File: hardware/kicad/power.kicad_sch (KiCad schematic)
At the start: 0 parts

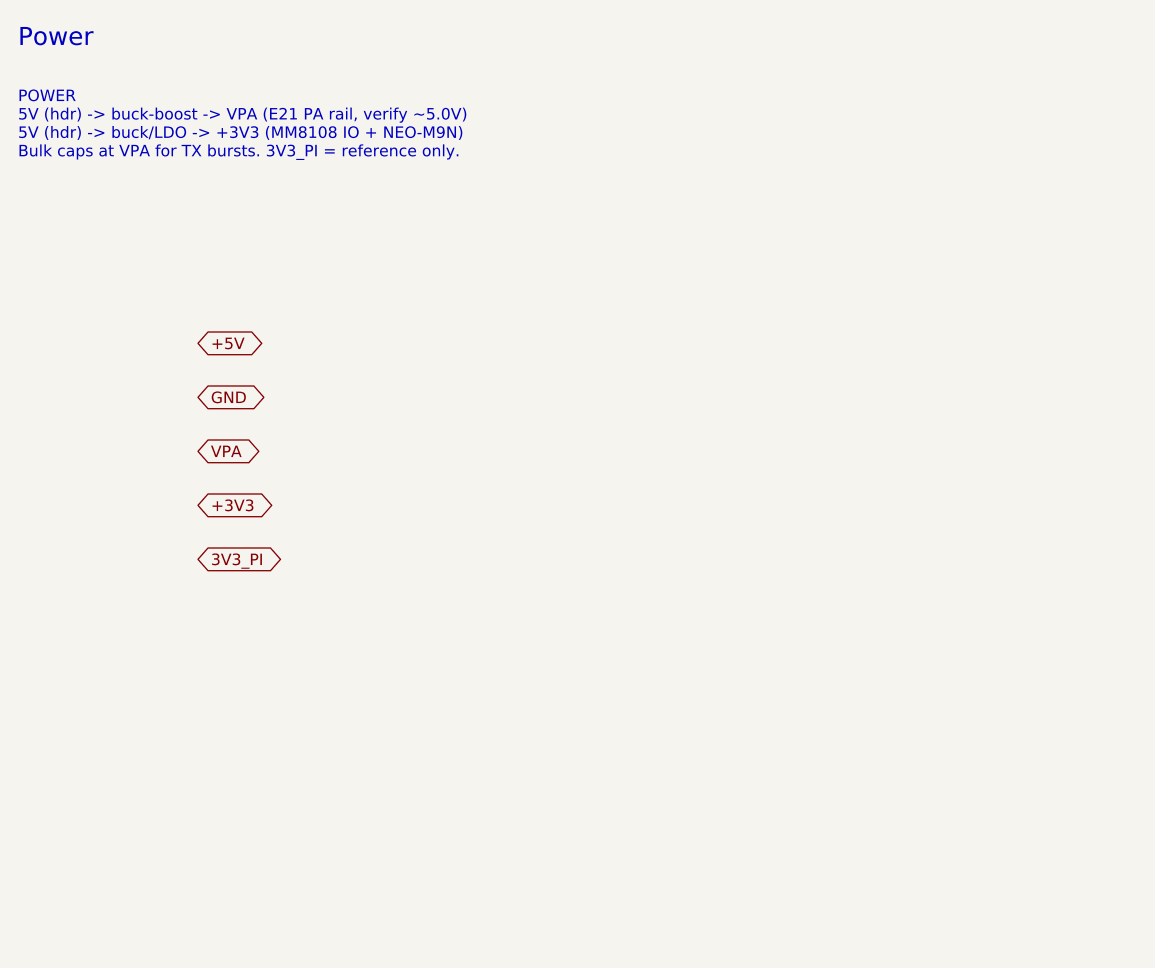
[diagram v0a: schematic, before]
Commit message: Deepen design to component level + fix EEPROM power rail
- Fix: HAT ID EEPROM (U6) now powered from Pi header 3V3 (3V3_PI, pin 1)
  so it is readable at boot before the HAT's own 3V3 comes up (was
  incorrectly on the HAT 3V3 regulator).
- Add docs/SCHEMATIC.md: component-level subcircuits for every block
  (refdes + values + nets) — buck-boost/3V3 FB dividers, MM8108 SPI
  termination/pulls, E21 RF DC-blocks/attenuator pad/T-R pulldowns,
  NEO-M9N active-antenna bias via VCC_RF, ID EEPROM (WP default).
- Add docs/BRINGUP.md: stage-gated power-on + RF test plan (don't key
  the 1W PA until rails/drive-level/FEM-timing verified).
- Add GNSS VCC_RF antenna bias + +3V3_GNSS ferrite to the net list.
- Enrich KiCad sub-sheets with per-block refdes notes and the new nets;
  regenerate scaffold (KiCad 10 format, S-expression balance re-checked).
- BOM: concrete passives (RF DC-blocks, attenuator pad, ferrite, TVS,
  FB dividers, WP jumper).

https://claude.ai/code/session_015nkkW85U3sPf5mcvrsMw7T
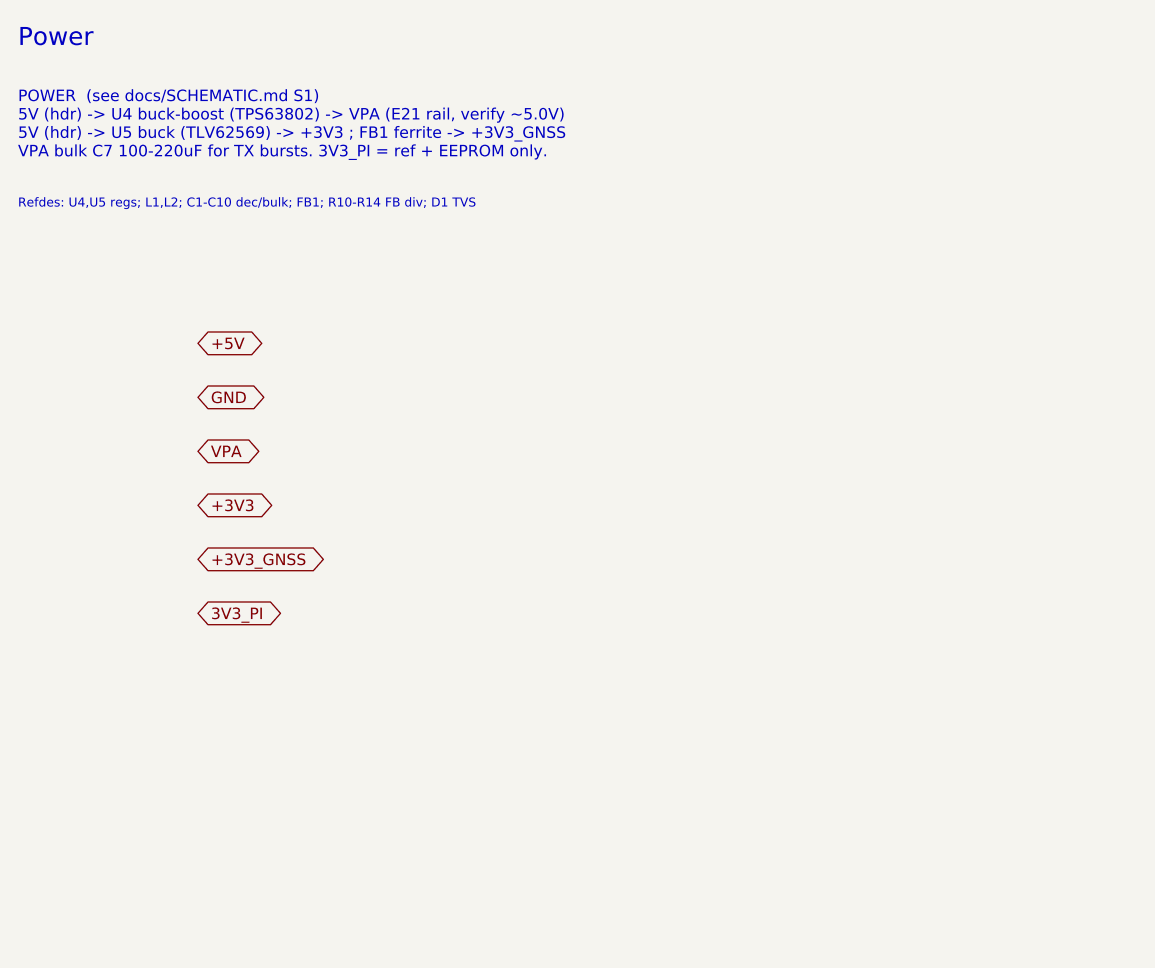
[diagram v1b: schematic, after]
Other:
- note added: "POWER (see docs/SCHEMATIC.md S1) 5V (hdr) -> U4 buck-boost (TPS63802) -> VPA (E21 rail, verify ~5.0V) 5V (hdr) -> U5 buck (TLV62569) -> +3V3 ; FB1 ferrite -> +3V3_GNSS VPA bulk C7 100-220uF for TX bursts. 3V3_PI = ref + EEPROM only."
- note added: "Refdes: U4,U5 regs; L1,L2; C1-C10 dec/bulk; FB1; R10-R14 FB div; D1 TVS"
- note removed: "POWER 5V (hdr) -> buck-boost -> VPA (E21 PA rail, verify ~5.0V) 5V (hdr) -> buck/LDO -> +3V3 (MM8108 IO + NEO-M9N) Bulk caps at VPA for TX bursts. 3V3_PI = reference only."
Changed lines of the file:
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@@
 	(paper "A4")
 	(text "Power" (exclude_from_sim no) (at 20 15 0) (effects (font (size 2 2) (thickness 0.3)) (justify left top)))
-	(text "POWER\n5V (hdr) -> buck-boost -> VPA (E21 PA rail, verify ~5.0V)\n5V (hdr) -> buck/LDO -> +3V3 (MM8108 IO + NEO-M9N)\nBulk caps at VPA for TX bursts. 3V3_PI = reference only." (exclude_from_sim no) (at 20 22 0) (effects (font (size 1.27 1.27)) (justify left top)))
+	(text "POWER  (see docs/SCHEMATIC.md S1)\n5V (hdr) -> U4 buck-boost (TPS63802) -> VPA (E21 rail, verify ~5.0V)\n5V (hdr) -> U5 buck (TLV62569) -> +3V3 ; FB1 ferrite -> +3V3_GNSS\nVPA bulk C7 100-220uF for TX bursts. 3V3_PI = ref + EEPROM only." (exclude_from_sim no) (at 20 22 0) (effects (font (size 1.27 1.27)) (justify left top)))
+	(text "Refdes: U4,U5 regs; L1,L2; C1-C10 dec/bulk; FB1; R10-R14 FB div; D1 TVS" (exclude_from_sim no) (at 20 34 0) (effects (font (size 1.0 1.0)) (justify left top)))
 	(global_label "+5V" (shape bidirectional) (at 40 50 0) (fields_autoplaced yes) (effects (font (size 1.27 1.27)) (justify left)))
 	(global_label "GND" (shape bidirectional) (at 40 56 0) (fields_autoplaced yes) (effects (font (size 1.27 1.27)) (justify left)))
 	(global_label "VPA" (shape bidirectional) (at 40 62 0) (fields_autoplaced yes) (effects (font (size 1.27 1.27)) (justify left)))
 	(global_label "+3V3" (shape bidirectional) (at 40 68 0) (fields_autoplaced yes) (effects (font (size 1.27 1.27)) (justify left)))
-	(global_label "3V3_PI" (shape bidirectional) (at 40 74 0) (fields_autoplaced yes) (effects (font (size 1.27 1.27)) (justify left)))
+	(global_label "+3V3_GNSS" (shape bidirectional) (at 40 74 0) (fields_autoplaced yes) (effects (font (size 1.27 1.27)) (justify left)))
+	(global_label "3V3_PI" (shape bidirectional) (at 40 80 0) (fields_autoplaced yes) (effects (font (size 1.27 1.27)) (justify left)))
 )

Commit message: Add gap-analysis components (datasheet-grounded) + RTC
Read the uploaded datasheets (MM8108-MF15457, E21-900G30S, NEO-M9N-00B)
and resolved the component gaps:

- #1/#2 RESOLVED by the module: MF15457 is self-contained (internal
  clock+PMU+PA); only needs VBAT/VBAT_TX/VDDIO 3.0-3.6 V. No external SoC
  inductors, 1V8/1V2 rails, or TCXO.
- VPA fixed at 5.0 V (E21 needs 4.75-5.25 V, ~620 mA TX, +20 dBm in ->
  +30 dBm out, 12 dB gain). Real pinouts wired (module 38-pin; E21
  pin6=PIN xcvr, pin9=ANT).
- Architecture finding: module has integrated PA + single ANT pin and NO
  hardware T/R FEM line. External E21 now needs (a) ~3-5 dB drive pad,
  (b) T/R control via module GPIO0/1 toggled by OpenMANET FW (or RF-sense
  auto-T/R fallback), and (c) end-product recertification at +30 dBm.

Added components:
- N3 900 MHz harmonic LPF (FL2); N4 inrush soft-start load switch (U10);
  N5 supervisor (U11); N6 radio-rail load switch (U12, OpenMANET
  power-gpios); N7 RF shields; N8 GNSS antenna ESD (D8); N9 status LEDs;
  N10 E21 thermal relief.
- RTC: RV-3028-C7 (U13) on I2C1 0x52 with a soldered rechargeable cell
  (BT1, trickle-charged) per request; added to the device-tree overlay.
- Declined per request: debug UART/JTAG pads, test points.

Updated docs (new COMPONENTS_GAP.md; DECISIONS B1-B9; SCHEMATIC; BOM;
POWER budget), netlist, overlay, and regenerated the KiCad 10 scaffold
with the new nets. Committed the vendor datasheets under hardware/.

https://claude.ai/code/session_015nkkW85U3sPf5mcvrsMw7T
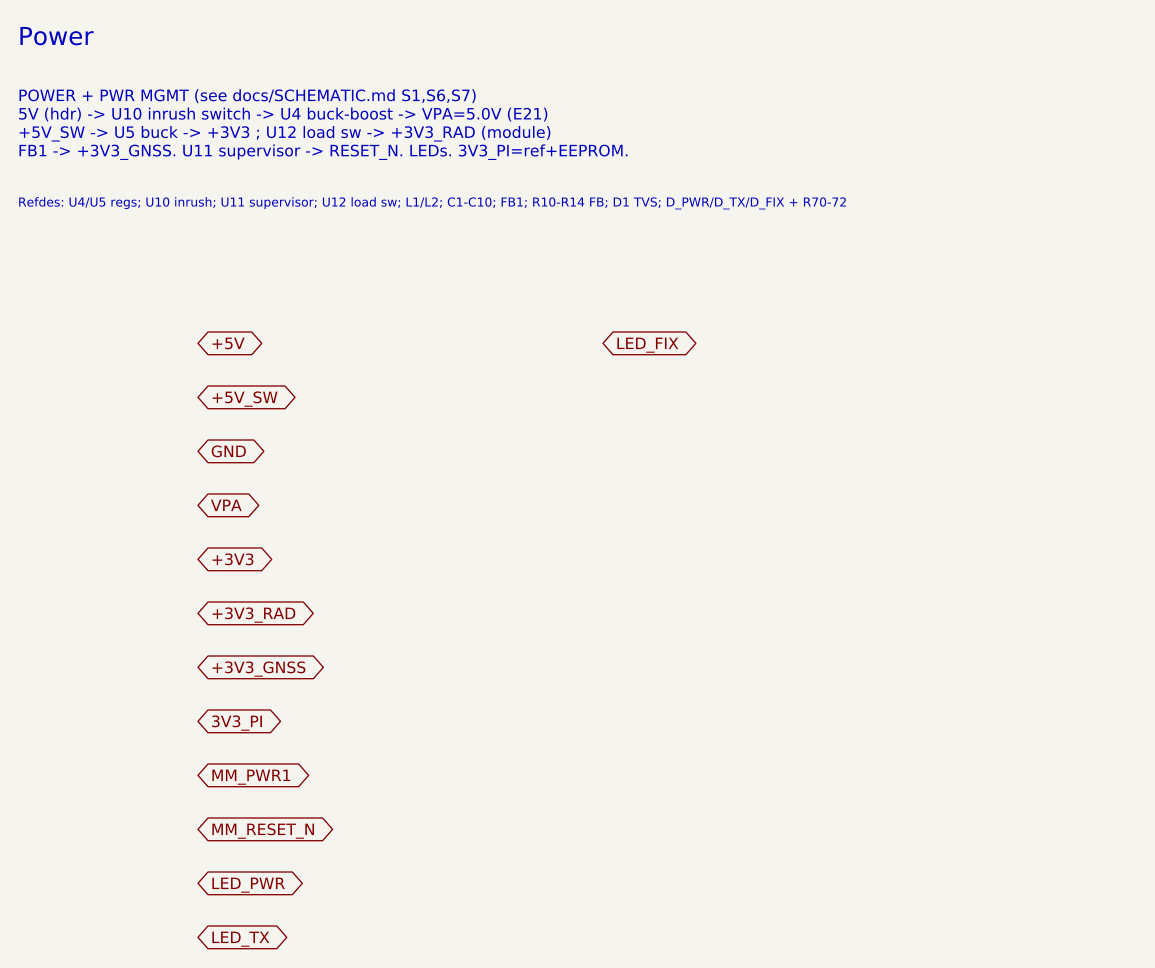
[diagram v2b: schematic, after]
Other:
- note added: "POWER + PWR MGMT (see docs/SCHEMATIC.md S1,S6,S7) 5V (hdr) -> U10 inrush switch -> U4 buck-boost -> VPA=5.0V (E21) +5V_SW -> U5 buck -> +3V3 ; U12 load sw -> +3V3_RAD (module) FB1 -> +3V3_GNSS. U11 supervisor -> RESET_N. LEDs. 3V3_PI=ref+EEPROM."
- note added: "Refdes: U4/U5 regs; U10 inrush; U11 supervisor; U12 load sw; L1/L2; C1-C10; FB1; R10-R14 FB; D1 TVS; D_PWR/D_TX/D_FIX + R70-72"
- note removed: "POWER (see docs/SCHEMATIC.md S1) 5V (hdr) -> U4 buck-boost (TPS63802) -> VPA (E21 rail, verify ~5.0V) 5V (hdr) -> U5 buck (TLV62569) -> +3V3 ; FB1 ferrite -> +3V3_GNSS VPA bulk C7 100-220uF for TX bursts. 3V3_PI = ref + EEPROM only."
- note removed: "Refdes: U4,U5 regs; L1,L2; C1-C10 dec/bulk; FB1; R10-R14 FB div; D1 TVS"
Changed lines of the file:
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@@
 	(paper "A4")
 	(text "Power" (exclude_from_sim no) (at 20 15 0) (effects (font (size 2 2) (thickness 0.3)) (justify left top)))
-	(text "POWER  (see docs/SCHEMATIC.md S1)\n5V (hdr) -> U4 buck-boost (TPS63802) -> VPA (E21 rail, verify ~5.0V)\n5V (hdr) -> U5 buck (TLV62569) -> +3V3 ; FB1 ferrite -> +3V3_GNSS\nVPA bulk C7 100-220uF for TX bursts. 3V3_PI = ref + EEPROM only." (exclude_from_sim no) (at 20 22 0) (effects (font (size 1.27 1.27)) (justify left top)))
-	(text "Refdes: U4,U5 regs; L1,L2; C1-C10 dec/bulk; FB1; R10-R14 FB div; D1 TVS" (exclude_from_sim no) (at 20 34 0) (effects (font (size 1.0 1.0)) (justify left top)))
+	(text "POWER + PWR MGMT (see docs/SCHEMATIC.md S1,S6,S7)\n5V (hdr) -> U10 inrush switch -> U4 buck-boost -> VPA=5.0V (E21)\n+5V_SW -> U5 buck -> +3V3 ; U12 load sw -> +3V3_RAD (module)\nFB1 -> +3V3_GNSS. U11 supervisor -> RESET_N. LEDs. 3V3_PI=ref+EEPROM." (exclude_from_sim no) (at 20 22 0) (effects (font (size 1.27 1.27)) (justify left top)))
+	(text "Refdes: U4/U5 regs; U10 inrush; U11 supervisor; U12 load sw; L1/L2; C1-C10; FB1; R10-R14 FB; D1 TVS; D_PWR/D_TX/D_FIX + R70-72" (exclude_from_sim no) (at 20 34 0) (effects (font (size 1.0 1.0)) (justify left top)))
 	(global_label "+5V" (shape bidirectional) (at 40 50 0) (fields_autoplaced yes) (effects (font (size 1.27 1.27)) (justify left)))
-	(global_label "GND" (shape bidirectional) (at 40 56 0) (fields_autoplaced yes) (effects (font (size 1.27 1.27)) (justify left)))
-	(global_label "VPA" (shape bidirectional) (at 40 62 0) (fields_autoplaced yes) (effects (font (size 1.27 1.27)) (justify left)))
-	(global_label "+3V3" (shape bidirectional) (at 40 68 0) (fields_autoplaced yes) (effects (font (size 1.27 1.27)) (justify left)))
-	(global_label "+3V3_GNSS" (shape bidirectional) (at 40 74 0) (fields_autoplaced yes) (effects (font (size 1.27 1.27)) (justify left)))
-	(global_label "3V3_PI" (shape bidirectional) (at 40 80 0) (fields_autoplaced yes) (effects (font (size 1.27 1.27)) (justify left)))
+	(global_label "+5V_SW" (shape bidirectional) (at 40 56 0) (fields_autoplaced yes) (effects (font (size 1.27 1.27)) (justify left)))
+	(global_label "GND" (shape bidirectional) (at 40 62 0) (fields_autoplaced yes) (effects (font (size 1.27 1.27)) (justify left)))
+	(global_label "VPA" (shape bidirectional) (at 40 68 0) (fields_autoplaced yes) (effects (font (size 1.27 1.27)) (justify left)))
+	(global_label "+3V3" (shape bidirectional) (at 40 74 0) (fields_autoplaced yes) (effects (font (size 1.27 1.27)) (justify left)))
+	(global_label "+3V3_RAD" (shape bidirectional) (at 40 80 0) (fields_autoplaced yes) (effects (font (size 1.27 1.27)) (justify left)))
+	(global_label "+3V3_GNSS" (shape bidirectional) (at 40 86 0) (fields_autoplaced yes) (effects (font (size 1.27 1.27)) (justify left)))
+	(global_label "3V3_PI" (shape bidirectional) (at 40 92 0) (fields_autoplaced yes) (effects (font (size 1.27 1.27)) (justify left)))
+	(global_label "MM_PWR1" (shape bidirectional) (at 40 98 0) (fields_autoplaced yes) (effects (font (size 1.27 1.27)) (justify left)))
+	(global_label "MM_RESET_N" (shape bidirectional) (at 40 104 0) (fields_autoplaced yes) (effects (font (size 1.27 1.27)) (justify left)))
+	(global_label "LED_PWR" (shape bidirectional) (at 40 110 0) (fields_autoplaced yes) (effects (font (size 1.27 1.27)) (justify left)))
+	(global_label "LED_TX" (shape bidirectional) (at 40 116 0) (fields_autoplaced yes) (effects (font (size 1.27 1.27)) (justify left)))
+	(global_label "LED_FIX" (shape bidirectional) (at 85 50 0) (fields_autoplaced yes) (effects (font (size 1.27 1.27)) (justify left)))
 )

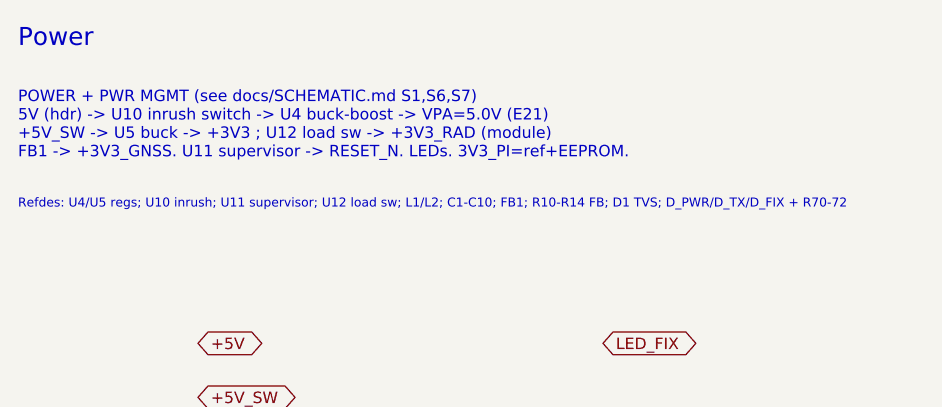
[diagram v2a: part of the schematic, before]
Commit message: Make E21 PA a DNP/optional Variant B; default to module-only
Deployment is ground/handheld/vehicle (NLOS), where the E21's +3 dB buys
only ~20% range (LINK_BUDGET) against ~620 mA + heat + recert + RX-rate
risk. So restructure as one PCB with two BOM builds:

- Variant A (DEFAULT): module-only ~27 dBm via OpenMANET BCF. E21,
  buck-boost (VPA), LPF and drive pad are DNP; an RF bypass (C_BYP)
  carries the module ANT straight to U.FL #2. Low power (~0.35 A), good
  for battery handhelds, stays on the module's modular cert.
- Variant B (OPTIONAL): populate E21 + VPA + LPF + T/R for +30 dBm
  extended range (fixed/elevated LoS); remove C_BYP; needs custom-BCF
  FEM GPIO control + end-product recert. No respin required.

Updated DECISIONS (B5/B10 resolved + new §C variants & order), SCHEMATIC,
POWER (default-build budget), BOM (variant tags + C_BYP), netlist, README,
and regenerated the KiCad scaffold (bypass net + silk tags).

https://claude.ai/code/session_015nkkW85U3sPf5mcvrsMw7T
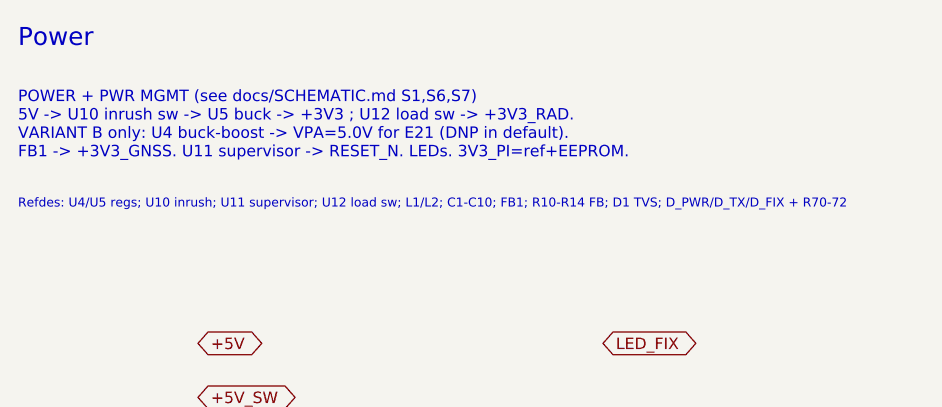
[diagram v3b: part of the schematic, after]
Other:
- note added: "POWER + PWR MGMT (see docs/SCHEMATIC.md S1,S6,S7) 5V -> U10 inrush sw -> U5 buck -> +3V3 ; U12 load sw -> +3V3_RAD. VARIANT B only: U4 buck-boost -> VPA=5.0V for E21 (DNP in default). FB1 -> +3V3_GNSS. U11 supervisor -> RESET_N. LEDs. 3V3_PI=ref+EEPROM."
- note removed: "POWER + PWR MGMT (see docs/SCHEMATIC.md S1,S6,S7) 5V (hdr) -> U10 inrush switch -> U4 buck-boost -> VPA=5.0V (E21) +5V_SW -> U5 buck -> +3V3 ; U12 load sw -> +3V3_RAD (module) FB1 -> +3V3_GNSS. U11 supervisor -> RESET_N. LEDs. 3V3_PI=ref+EEPROM."
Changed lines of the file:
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@@
 	(paper "A4")
 	(text "Power" (exclude_from_sim no) (at 20 15 0) (effects (font (size 2 2) (thickness 0.3)) (justify left top)))
-	(text "POWER + PWR MGMT (see docs/SCHEMATIC.md S1,S6,S7)\n5V (hdr) -> U10 inrush switch -> U4 buck-boost -> VPA=5.0V (E21)\n+5V_SW -> U5 buck -> +3V3 ; U12 load sw -> +3V3_RAD (module)\nFB1 -> +3V3_GNSS. U11 supervisor -> RESET_N. LEDs. 3V3_PI=ref+EEPROM." (exclude_from_sim no) (at 20 22 0) (effects (font (size 1.27 1.27)) (justify left top)))
+	(text "POWER + PWR MGMT (see docs/SCHEMATIC.md S1,S6,S7)\n5V -> U10 inrush sw -> U5 buck -> +3V3 ; U12 load sw -> +3V3_RAD.\nVARIANT B only: U4 buck-boost -> VPA=5.0V for E21 (DNP in default).\nFB1 -> +3V3_GNSS. U11 supervisor -> RESET_N. LEDs. 3V3_PI=ref+EEPROM." (exclude_from_sim no) (at 20 22 0) (effects (font (size 1.27 1.27)) (justify left top)))
 	(text "Refdes: U4/U5 regs; U10 inrush; U11 supervisor; U12 load sw; L1/L2; C1-C10; FB1; R10-R14 FB; D1 TVS; D_PWR/D_TX/D_FIX + R70-72" (exclude_from_sim no) (at 20 34 0) (effects (font (size 1.0 1.0)) (justify left top)))
 	(global_label "+5V" (shape bidirectional) (at 40 50 0) (fields_autoplaced yes) (effects (font (size 1.27 1.27)) (justify left)))
